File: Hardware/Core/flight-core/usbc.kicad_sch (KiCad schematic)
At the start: 8 parts, among them J402 USB_C_Receptacle_USB2.0_16P, Q401 2N7002E, U403 USBLC6-2SC6

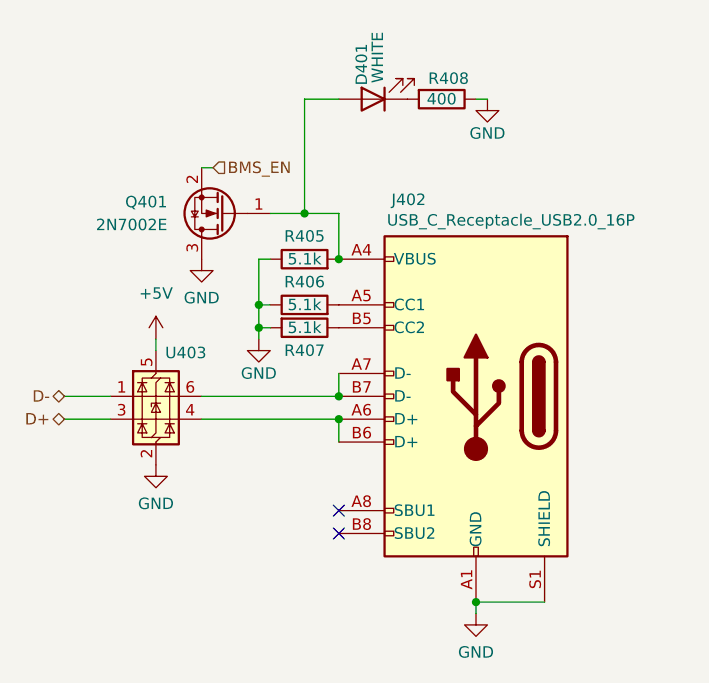
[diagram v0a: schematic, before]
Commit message: added 5V to USBC VBUS to power by usb; edited stm32 file to match
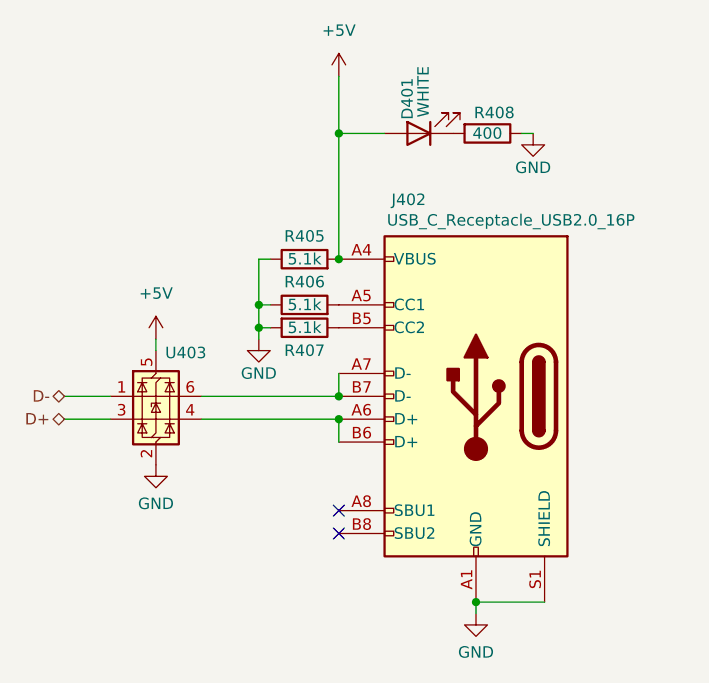
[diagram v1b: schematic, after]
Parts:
- removed Q401: 2N7002E, Package_TO_SOT_SMD:SOT-23, symbol Transistor_FET:2N7002E
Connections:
- net +5V: now also D401.2 (A), J402.A4 (VBUS), J402.A9 (VBUS), J402.B4 (VBUS), J402.B9 (VBUS), R405.2
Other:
- moved on the sheet: D401, R408
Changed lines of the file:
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@@
+	)
+	(junction
+		(at 143.51 69.85)
+		(diameter 0)
+		(color 0 0 0 0)
 	)
 	(junction
@@
 	)
 	(junction
-		(at 139.7 78.74)
-		(diameter 0)
-		(color 0 0 0 0)
-	)
-	(junction
 		(at 158.75 121.92)
 		(diameter 0)
@@
 	(wire
 		(pts
-			(xy 143.51 66.04) (xy 139.7 66.04)
+			(xy 143.51 69.85) (xy 148.59 69.85)
 		)
 		(stroke
@@
 	(wire
 		(pts
-			(xy 139.7 66.04) (xy 139.7 78.74)
-		)
-		(stroke
-			(width 0)
-			(type default)
-		)
-	)
-	(wire
-		(pts
-			(xy 143.51 78.74) (xy 143.51 83.82)
+			(xy 143.51 63.5) (xy 143.51 69.85)
 		)
 		(stroke
@@
 	(wire
 		(pts
-			(xy 135.89 78.74) (xy 139.7 78.74)
-		)
-		(stroke
-			(width 0)
-			(type default)
-		)
-	)
-	(wire
-		(pts
 			(xy 113.03 99.06) (xy 118.11 99.06)
 		)
@@
 	(wire
 		(pts
-			(xy 139.7 78.74) (xy 143.51 78.74)
-		)
-		(stroke
-			(width 0)
-			(type default)
-		)
-	)
-	(wire
-		(pts
 			(xy 158.75 121.92) (xy 166.37 121.92)
 		)
@@
 	(wire
 		(pts
-			(xy 160.02 66.04) (xy 158.75 66.04)
+			(xy 165.1 69.85) (xy 163.83 69.85)
 		)
 		(stroke
@@
 	(wire
 		(pts
+			(xy 143.51 69.85) (xy 143.51 83.82)
+		)
+		(stroke
+			(width 0)
+			(type default)
+		)
+	)
+	(wire
+		(pts
 			(xy 158.75 121.92) (xy 158.75 123.19)
 		)
@@
 			(width 0)
 			(type default)
-		)
-	)
-	(wire
-		(pts
-			(xy 129.54 73.66) (xy 128.27 73.66)
-		)
-		(stroke
-			(width 0)
-			(type default)
-		)
-	)
-	(hierarchical_label "BMS_EN"
-		(shape input)
-		(at 129.54 73.66 0)
-		(effects
-			(font
-				(size 1.27 1.27)
-			)
-			(justify left)
 		)
 	)
@@
 	(symbol
 		(lib_id "Device:LED")
-		(at 147.32 66.04 180)
+		(at 152.4 69.85 180)
 		(unit 1)
 		(exclude_from_sim no)
@@
 		(dnp no)
 		(property "Reference" "D401"
-			(at 146.05 64.516 90)
+			(at 151.13 68.326 90)
 			(effects
 				(font
@@
 		)
 		(property "Value" "WHITE"
-			(at 147.828 64.262 90)
+			(at 152.908 68.072 90)
 			(effects
 				(font
@@
 		)
 		(property "Footprint" "LED_SMD:LED_0805_2012Metric"
-			(at 147.32 66.04 0)
+			(at 152.4 69.85 0)
 			(effects
 				(font
@@
 		)
 		(property "Datasheet" "~"
-			(at 147.32 66.04 0)
+			(at 152.4 69.85 0)
 			(effects
 				(font
@@
 		)
 		(property "Description" "Light emitting diode"
-			(at 147.32 66.04 0)
+			(at 152.4 69.85 0)
 			(effects
 				(font
@@
 	)
 	(symbol
-		(lib_name "GND_4")
-		(lib_id "power:GND")
-		(at 128.27 83.82 0)
-		(unit 1)
-		(exclude_from_sim no)
-		(in_bom yes)
-		(on_board yes)
-		(dnp no)
-		(property "Reference" "#PWR0424"
-			(at 128.27 90.17 0)
-			(effects
-				(font
-					(size 1.27 1.27)
-				)
-				(hide yes)
-			)
-		)
-		(property "Value" "GND"
-			(at 128.27 88.138 0)
-			(effects
-				(font
-					(size 1.27 1.27)
-				)
-			)
-		)
-		(property "Footprint" ""
-			(at 128.27 83.82 0)
-			(effects
-				(font
-					(size 1.27 1.27)
-				)
-				(hide yes)
-			)
-		)
-		(property "Datasheet" ""
-			(at 128.27 83.82 0)
-			(effects
-				(font
-					(size 1.27 1.27)
-				)
-				(hide yes)
-			)
-		)
-		(property "Description" "Power symbol creates a global label with name \"GND\" , ground"
-			(at 128.27 83.82 0)
-			(effects
-				(font
-					(size 1.27 1.27)
-				)
-				(hide yes)
-			)
-		)
-		(pin "1"
-		)
-		(instances
-			(project "flight-core"
-				(path "/93f46f4b-cdf5-47ec-af03-96378e73b2e1/91e18f07-bd3f-4576-bbe1-a0227cf7132e/18962740-1c79-42a0-bb7c-73bce74e5c8a"
-					(reference "#PWR0424")
-					(unit 1)
-				)
-			)
-		)
-	)
-	(symbol
 		(lib_id "Device:R")
-		(at 154.94 66.04 270)
+		(at 160.02 69.85 270)
 		(unit 1)
 		(exclude_from_sim no)
@@
 		(dnp no)
 		(property "Reference" "R408"
-			(at 155.702 63.754 90)
+			(at 160.782 67.564 90)
 			(effects
 				(font
@@
 		)
 		(property "Value" "400"
-			(at 154.94 66.04 90)
+			(at 160.02 69.85 90)
 			(effects
 				(font
@@
 		)
 		(property "Footprint" "Resistor_SMD:R_0603_1608Metric"
-			(at 154.94 64.262 90)
+			(at 160.02 68.072 90)
 			(effects
 				(font
@@
 		)
 		(property "Datasheet" "~"
-			(at 154.94 66.04 0)
+			(at 160.02 69.85 0)
 			(effects
 				(font
@@
 		)
 		(property "Description" "Resistor"
-			(at 154.94 66.04 0)
+			(at 160.02 69.85 0)
 			(effects
 				(font
@@
 		(lib_name "GND_4")
 		(lib_id "power:GND")
-		(at 160.02 66.04 0)
+		(at 165.1 69.85 0)
 		(unit 1)
 		(exclude_from_sim no)
@@
 		(dnp no)
 		(property "Reference" "#PWR0431"
-			(at 160.02 72.39 0)
+			(at 165.1 76.2 0)
 			(effects
 				(font
@@
 		)
 		(property "Value" "GND"
-			(at 160.02 69.85 0)
+			(at 165.1 73.66 0)
 			(effects
 				(font
@@
 		)
 		(property "Footprint" ""
-			(at 160.02 66.04 0)
+			(at 165.1 69.85 0)
 			(effects
 				(font
@@
 		)
 		(property "Datasheet" ""
-			(at 160.02 66.04 0)
+			(at 165.1 69.85 0)
 			(effects
 				(font
@@
 		)
 		(property "Description" "Power symbol creates a global label with name \"GND\" , ground"
-			(at 160.02 66.04 0)
+			(at 165.1 69.85 0)
 			(effects
 				(font
@@
 	)
 	(symbol
-		(lib_id "Transistor_FET:2N7002E")
-		(at 130.81 78.74 180)
+		(lib_name "+5V_1")
+		(lib_id "power:+5V")
+		(at 143.51 63.5 0)
 		(unit 1)
 		(exclude_from_sim no)
@@
 		(dnp no)
 		(fields_autoplaced yes)
-		(property "Reference" "Q401"
-			(at 124.46 77.4699 0)
-			(effects
-				(font
-					(size 1.27 1.27)
-				)
-				(justify left)
-			)
-		)
-		(property "Value" "2N7002E"
-			(at 124.46 80.0099 0)
-			(effects
-				(font
-					(size 1.27 1.27)
-				)
-				(justify left)
-			)
-		)
-		(property "Footprint" "Package_TO_SOT_SMD:SOT-23"
-			(at 125.73 76.835 0)
-			(effects
-				(font
-					(size 1.27 1.27)
-					(italic yes)
-				)
-				(justify left)
-				(hide yes)
-			)
-		)
-		(property "Datasheet" "http://www.diodes.com/assets/Datasheets/ds30376.pdf"
-			(at 125.73 74.93 0)
-			(effects
-				(font
-					(size 1.27 1.27)
-				)
-				(justify left)
-				(hide yes)
-			)
-		)
-		(property "Description" "0.24A Id, 60V Vds, N-Channel MOSFET, SOT-23"
-			(at 130.81 78.74 0)
-			(effects
-				(font
-					(size 1.27 1.27)
-				)
-				(hide yes)
-			)
-		)
-		(pin "3"
+		(property "Reference" "#PWR0346"
+			(at 143.51 67.31 0)
+			(effects
+				(font
+					(size 1.27 1.27)
+				)
+				(hide yes)
+			)
+		)
+		(property "Value" "+5V"
+			(at 143.51 58.42 0)
+			(effects
+				(font
+					(size 1.27 1.27)
+				)
+			)
+		)
+		(property "Footprint" ""
+			(at 143.51 63.5 0)
+			(effects
+				(font
+					(size 1.27 1.27)
+				)
+				(hide yes)
+			)
+		)
+		(property "Datasheet" ""
+			(at 143.51 63.5 0)
+			(effects
+				(font
+					(size 1.27 1.27)
+				)
+				(hide yes)
+			)
+		)
+		(property "Description" "Power symbol creates a global label with name \"+5V\""
+			(at 143.51 63.5 0)
+			(effects
+				(font
+					(size 1.27 1.27)
+				)
+				(hide yes)
+			)
 		)
 		(pin "1"
-		)
-		(pin "2"
 		)
 		(instances
 			(project "flight-core"
 				(path "/93f46f4b-cdf5-47ec-af03-96378e73b2e1/91e18f07-bd3f-4576-bbe1-a0227cf7132e/18962740-1c79-42a0-bb7c-73bce74e5c8a"
-					(reference "Q401")
+					(reference "#PWR0346")
 					(unit 1)
 				)

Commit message: removed 5.1k resistor to eliminate usb logic
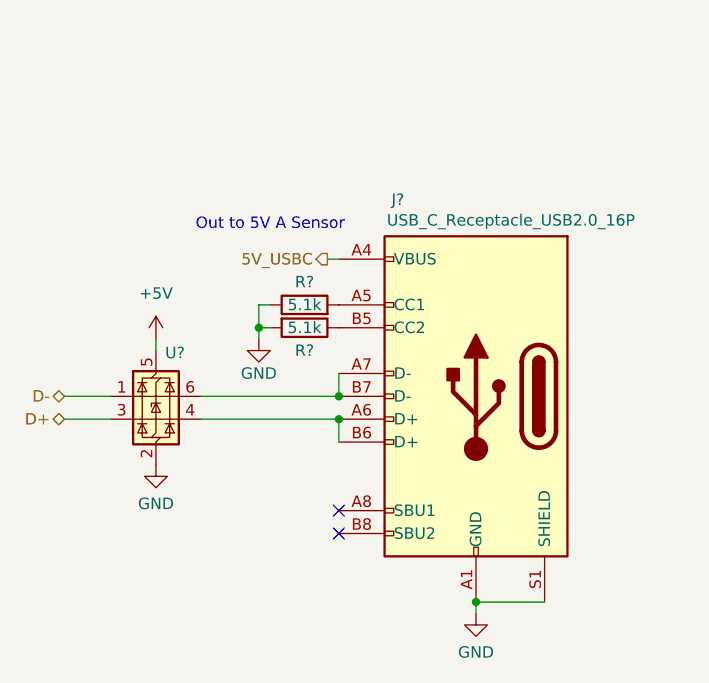
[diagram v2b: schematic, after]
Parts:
- removed D401: WHITE, LED_SMD:LED_0805_2012Metric, symbol Device:LED
- removed R405: 5.1k, OEM:R_0603_1608Metric, symbol OEM:1KR
- removed R408: 400, Resistor_SMD:R_0603_1608Metric, symbol Device:R
- renumbered J402 to J?, R406 to R?, R407 to R?, U403 to U?
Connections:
- net +5V: no longer J?.A4 (VBUS), J?.A9 (VBUS), J?.B4 (VBUS), J?.B9 (VBUS)
- new net 5V_USBC: J?.A4 (VBUS), J?.A9 (VBUS), J?.B4 (VBUS), J?.B9 (VBUS)
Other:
- note added: "Out to 5V A Sensor"

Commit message: minor erc fixes (grid, reannotation, updated footprint associations)
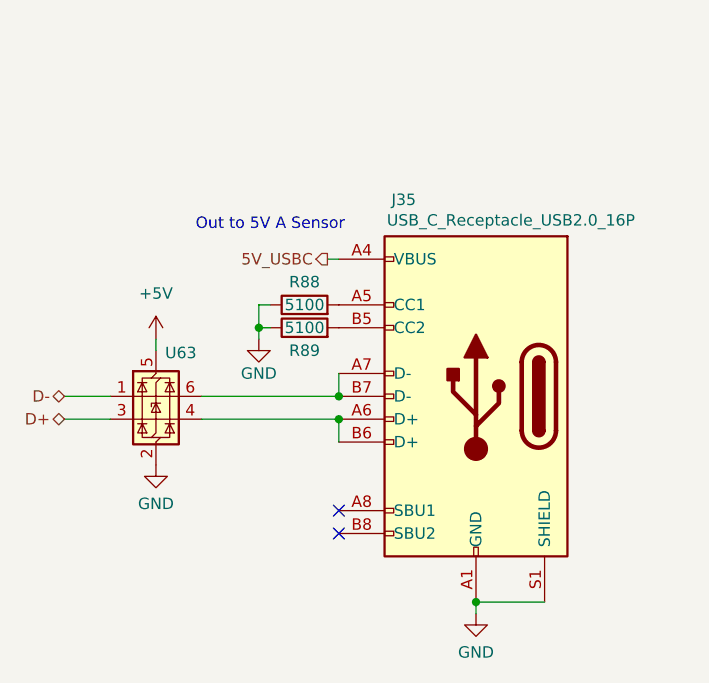
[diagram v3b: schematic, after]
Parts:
- removed R? (x2): 5.1k, OEM:R_0603_1608Metric, symbol OEM:1KR
- added R88, R89: 5100, footprints:R_0603_1608Metric, symbol Device:R
- gave numbers to parts that had none: 2
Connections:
- net GND: now also R88.1, R89.1
- net at J35.A5 (CC1): now also R88.2
- net at J35.B5 (CC2): now also R89.2
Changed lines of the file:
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@@
 		(on_board yes)
 		(dnp no)
-		(property "Reference" "#PWR?"
+		(property "Reference" "#PWR0293"
 			(at 134.62 99.06 0)
 			(effects
@@
 			(project "usbc"
 				(path "/93f46f4b-cdf5-47ec-af03-96378e73b2e1/91e18f07-bd3f-4576-bbe1-a0227cf7132e/dc9c6c82-2ca0-4595-949b-0b07300fa078"
-					(reference "#PWR?")
+					(reference "#PWR0293")
 					(unit 1)
 				)
@@
 		(on_board yes)
 		(dnp no)
-		(property "Reference" "U?"
+		(property "Reference" "U63"
 			(at 124.206 94.234 0)
 			(effects
@@
 			(project "usbc"
 				(path "/93f46f4b-cdf5-47ec-af03-96378e73b2e1/91e18f07-bd3f-4576-bbe1-a0227cf7132e/dc9c6c82-2ca0-4595-949b-0b07300fa078"
-					(reference "U?")
+					(reference "U63")
 					(unit 1)
 				)
@@
 		(on_board yes)
 		(dnp no)
-		(property "Reference" "#PWR?"
+		(property "Reference" "#PWR0294"
 			(at 158.75 129.54 0)
 			(effects
@@
 			(project "usbc"
 				(path "/93f46f4b-cdf5-47ec-af03-96378e73b2e1/91e18f07-bd3f-4576-bbe1-a0227cf7132e/dc9c6c82-2ca0-4595-949b-0b07300fa078"
-					(reference "#PWR?")
+					(reference "#PWR0294")
 					(unit 1)
 				)
@@
 		(on_board yes)
 		(dnp no)
-		(property "Reference" "J?"
+		(property "Reference" "J35"
 			(at 149.352 77.216 0)
 			(effects
@@
 			(project "usbc"
 				(path "/93f46f4b-cdf5-47ec-af03-96378e73b2e1/91e18f07-bd3f-4576-bbe1-a0227cf7132e/dc9c6c82-2ca0-4595-949b-0b07300fa078"
-					(reference "J?")
+					(reference "J35")
 					(unit 1)
 				)
@@
 		(dnp no)
 		(fields_autoplaced yes)
-		(property "Reference" "#PWR?"
+		(property "Reference" "#PWR0291"
 			(at 123.19 96.52 0)
 			(effects
@@
 			(project "usbc"
 				(path "/93f46f4b-cdf5-47ec-af03-96378e73b2e1/91e18f07-bd3f-4576-bbe1-a0227cf7132e/dc9c6c82-2ca0-4595-949b-0b07300fa078"
-					(reference "#PWR?")
-					(unit 1)
-				)
-			)
-		)
-	)
-	(symbol
-		(lib_id "OEM:1KR")
+					(reference "#PWR0291")
+					(unit 1)
+				)
+			)
+		)
+	)
+	(symbol
+		(lib_id "Device:R")
 		(at 139.7 88.9 90)
 		(unit 1)
@@
 		(on_board yes)
 		(dnp no)
-		(property "Reference" "R?"
+		(property "Reference" "R88"
 			(at 139.7 86.36 90)
 			(effects
@@
 			)
 		)
-		(property "Value" "5.1k"
+		(property "Value" "5100"
 			(at 139.7 88.9 90)
 			(effects
@@
 			)
 		)
-		(property "Footprint" "OEM:R_0603_1608Metric"
-			(at 139.7 90.678 0)
-			(effects
-				(font
-					(size 1.27 1.27)
-				)
-				(hide yes)
-			)
-		)
-		(property "Datasheet" "${OEM_DIR}/parts/datasheets/stackpole_RMCF_RMCP.pdf"
-			(at 139.7 86.868 0)
-			(effects
-				(font
-					(size 1.27 1.27)
-				)
-				(hide yes)
-			)
-		)
-		(property "Description" ""
+		(property "Footprint" "footprints:R_0603_1608Metric"
+			(at 139.7 90.678 90)
+			(effects
+				(font
+					(size 1.27 1.27)
+				)
+				(hide yes)
+			)
+		)
+		(property "Datasheet" "~"
 			(at 139.7 88.9 0)
 			(effects
@@
 			)
 		)
-		(property "MFN" "Stackpole Electronics"
+		(property "Description" "Resistor"
 			(at 139.7 88.9 0)
 			(effects
 				(font
-					(size 1.524 1.524)
-				)
-				(hide yes)
-			)
-		)
-		(property "MPN" "RMCF0603FT1K00"
-			(at 139.7 88.9 0)
-			(effects
-				(font
-					(size 1.524 1.524)
-				)
-				(hide yes)
-			)
-		)
-		(property "DKPN" "RMCF0603FT1K00TR-ND"
-			(at 139.7 88.9 0)
-			(effects
-				(font
-					(size 1.27 1.27)
-				)
-				(hide yes)
-			)
-		)
-		(property "NewDesigns" "YES"
-			(at 139.7 88.9 0)
-			(effects
-				(font
-					(size 1.27 1.27)
-				)
-				(hide yes)
-			)
-		)
-		(property "Stocked" "Reel"
-			(at 139.7 88.9 0)
-			(effects
-				(font
-					(size 1.27 1.27)
-				)
-				(hide yes)
-			)
-		)
-		(property "Package" "0603"
-			(at 139.7 88.9 0)
-			(effects
-				(font
-					(size 1.27 1.27)
-				)
-				(hide yes)
-			)
-		)
-		(property "Style" "SMD"
-			(at 139.7 88.9 0)
-			(effects
-				(font
 					(size 1.27 1.27)
 				)
@@
 		)
 		(instances
-			(project "usbc"
-				(path "/5b2d7450-9def-4ea1-9c70-a6272bc3923e"
-					(reference "R?")
-					(unit 1)
-				)
-			)
-			(project "usbc"
-				(path "/93f46f4b-cdf5-47ec-af03-96378e73b2e1/91e18f07-bd3f-4576-bbe1-a0227cf7132e/dc9c6c82-2ca0-4595-949b-0b07300fa078"
-					(reference "R?")
+			(project ""
+				(path "/93f46f4b-cdf5-47ec-af03-96378e73b2e1/91e18f07-bd3f-4576-bbe1-a0227cf7132e/dc9c6c82-2ca0-4595-949b-0b07300fa078"
+					(reference "R88")
+					(unit 1)
+				)
+			)
+		)
+	)
+	(symbol
+		(lib_id "Device:R")
+		(at 139.7 91.44 90)
+		(unit 1)
+		(exclude_from_sim no)
+		(in_bom yes)
+		(on_board yes)
+		(dnp no)
+		(property "Reference" "R89"
+			(at 139.7 93.98 90)
+			(effects
+				(font
+					(size 1.27 1.27)
+				)
+			)
+		)
+		(property "Value" "5100"
+			(at 139.7 91.44 90)
+			(effects
+				(font
+					(size 1.27 1.27)
+				)
+			)
+		)
+		(property "Footprint" "footprints:R_0603_1608Metric"
+			(at 139.7 93.218 90)
+			(effects
+				(font
+					(size 1.27 1.27)
+				)
+				(hide yes)
+			)
+		)
+		(property "Datasheet" "~"
+			(at 139.7 91.44 0)
+			(effects
+				(font
+					(size 1.27 1.27)
+				)
+				(hide yes)
+			)
+		)
+		(property "Description" "Resistor"
+			(at 139.7 91.44 0)
+			(effects
+				(font
+					(size 1.27 1.27)
+				)
+				(hide yes)
+			)
+		)
+		(pin "1"
+		)
+		(pin "2"
+		)
+		(instances
+			(project "flight-core"
+				(path "/93f46f4b-cdf5-47ec-af03-96378e73b2e1/91e18f07-bd3f-4576-bbe1-a0227cf7132e/dc9c6c82-2ca0-4595-949b-0b07300fa078"
+					(reference "R89")
 					(unit 1)
 				)
@@
 		(on_board yes)
 		(dnp no)
-		(property "Reference" "#PWR?"
+		(property "Reference" "#PWR0292"
 			(at 123.19 113.03 0)
 			(effects
@@
 			(project "usbc"
 				(path "/93f46f4b-cdf5-47ec-af03-96378e73b2e1/91e18f07-bd3f-4576-bbe1-a0227cf7132e/dc9c6c82-2ca0-4595-949b-0b07300fa078"
-					(reference "#PWR?")
-					(unit 1)
-				)
-			)
-		)
-	)
-	(symbol
-		(lib_id "OEM:1KR")
-		(at 139.7 91.44 270)
-		(unit 1)
-		(exclude_from_sim no)
-		(in_bom yes)
-		(on_board yes)
-		(dnp no)
-		(property "Reference" "R?"
-			(at 139.7 93.98 90)
-			(effects
-				(font
-					(size 1.27 1.27)
-				)
-			)
-		)
-		(property "Value" "5.1k"
-			(at 139.7 91.44 90)
-			(effects
-				(font
-					(size 1.27 1.27)
-				)
-			)
-		)
-		(property "Footprint" "OEM:R_0603_1608Metric"
-			(at 139.7 89.662 0)
-			(effects
-				(font
-					(size 1.27 1.27)
-				)
-				(hide yes)
-			)
-		)
-		(property "Datasheet" "${OEM_DIR}/parts/datasheets/stackpole_RMCF_RMCP.pdf"
-			(at 139.7 93.472 0)
-			(effects
-				(font
-					(size 1.27 1.27)
-				)
-				(hide yes)
-			)
-		)
-		(property "Description" ""
-			(at 139.7 91.44 0)
-			(effects
-				(font
-					(size 1.27 1.27)
-				)
-				(hide yes)
-			)
-		)
-		(property "MFN" "Stackpole Electronics"
-			(at 139.7 91.44 0)
-			(effects
-				(font
-					(size 1.524 1.524)
-				)
-				(hide yes)
-			)
-		)
-		(property "MPN" "RMCF0603FT1K00"
-			(at 139.7 91.44 0)
-			(effects
-				(font
-					(size 1.524 1.524)
-				)
-				(hide yes)
-			)
-		)
-		(property "DKPN" "RMCF0603FT1K00TR-ND"
-			(at 139.7 91.44 0)
-			(effects
-				(font
-					(size 1.27 1.27)
-				)
-				(hide yes)
-			)
-		)
-		(property "NewDesigns" "YES"
-			(at 139.7 91.44 0)
-			(effects
-				(font
-					(size 1.27 1.27)
-				)
-				(hide yes)
-			)
-		)
-		(property "Stocked" "Reel"
-			(at 139.7 91.44 0)
-			(effects
-				(font
-					(size 1.27 1.27)
-				)
-				(hide yes)
-			)
-		)
-		(property "Package" "0603"
-			(at 139.7 91.44 0)
-			(effects
-				(font
-					(size 1.27 1.27)
-				)
-				(hide yes)
-			)
-		)
-		(property "Style" "SMD"
-			(at 139.7 91.44 0)
-			(effects
-				(font
-					(size 1.27 1.27)
-				)
-				(hide yes)
-			)
-		)
-		(pin "1"
-		)
-		(pin "2"
-		)
-		(instances
-			(project "usbc"
-				(path "/5b2d7450-9def-4ea1-9c70-a6272bc3923e"
-					(reference "R?")
-					(unit 1)
-				)
-			)
-			(project "usbc"
-				(path "/93f46f4b-cdf5-47ec-af03-96378e73b2e1/91e18f07-bd3f-4576-bbe1-a0227cf7132e/dc9c6c82-2ca0-4595-949b-0b07300fa078"
-					(reference "R?")
-					(unit 1)
-				)
+					(reference "#PWR0292")
+					(unit 1)
+				)
